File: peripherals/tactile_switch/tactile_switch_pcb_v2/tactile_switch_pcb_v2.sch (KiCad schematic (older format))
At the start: 3 parts, among them J1 PJ320A, SW1 SW_Push

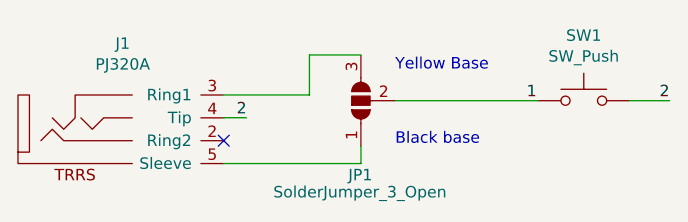
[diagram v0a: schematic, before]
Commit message: Increased tactile switch PCB hole diameters   - increased hole diameters to 1.2mm to accommodate pins     on 12mm x 12mm tactile switches.
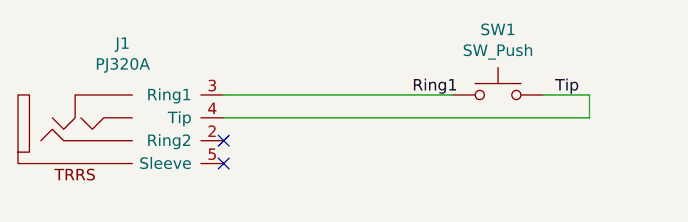
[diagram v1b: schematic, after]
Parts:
- removed JP1: SolderJumper_3_Open, Jumper:SolderJumper-3_P1.3mm_Open_RoundedPad1.0x1.5mm, symbol Jumper:SolderJumper_3_Open
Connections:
- net 1 is gone; now on net Ring1: SW1.1
- net Ring1: now reaches J1.3 (Ring1)
- net 2 renamed Tip
- no-connect marks 1 -> 2
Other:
- note removed: "Black base"
- note removed: "Yellow Base"
- moved on the sheet: SW1
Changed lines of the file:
@@
 EESchema Schematic File Version 4
-LIBS:tactile_switch_pcb_v2-cache
 EELAYER 30 0
 EELAYER END
@@
 L Switch:SW_Push SW1
 U 1 1 5D3251E9
-P 5950 3575
-F 0 "SW1" H 5950 3860 50  0000 C CNN
-F 1 "SW_Push" H 5950 3769 50  0000 C CNN
-F 2 "dbh_kicad_library:dbh_SW_PUSH-12mm" H 5950 3775 50  0001 C CNN
-F 3 "~" H 5950 3775 50  0001 C CNN
-	1    5950 3575
+P 5575 3550
+F 0 "SW1" H 5575 3835 50  0000 C CNN
+F 1 "SW_Push" H 5575 3744 50  0000 C CNN
+F 2 "dbh_kicad_library:dbh_SW_PUSH-12mm" H 5575 3750 50  0001 C CNN
+F 3 "~" H 5575 3750 50  0001 C CNN
+	1    5575 3550
 	1    0    0    -1
 $EndComp
-Wire Wire Line
-	6150 3575 6325 3575
-Text Label 6325 3575 2    50   ~ 0
-2
 $Comp
 L dbh_kicad_library:PJ320A J1
@@
 	1    0    0    -1
 $EndComp
+NoConn ~ 4375 3750
+Text Label 5200 3550 0    50   ~ 0
+Ring1
+NoConn ~ 4375 3850
 Wire Wire Line
-	4375 3650 4475 3650
-Text Label 4475 3650 2    50   ~ 0
-2
-NoConn ~ 4375 3750
-$Comp
-L Jumper:SolderJumper_3_Open JP1
-U 1 1 5D8354D3
-P 4975 3575
-F 0 "JP1" V 4650 3525 50  0000 L CNN
-F 1 "SolderJumper_3_Open" V 4575 3200 50  0000 L CNN
-F 2 "Jumper:SolderJumper-3_P1.3mm_Open_RoundedPad1.0x1.5mm" H 4975 3575 50  0001 C CNN
-F 3 "~" H 4975 3575 50  0001 C CNN
-	1    4975 3575
-	0    -1   -1   0
-$EndComp
+	4375 3550 5375 3550
 Wire Wire Line
-	5125 3575 5750 3575
+	5775 3550 5975 3550
 Wire Wire Line
-	4375 3550 4750 3550
+	5975 3550 5975 3650
 Wire Wire Line
-	4750 3550 4750 3375
-Wire Wire Line
-	4750 3375 4975 3375
-Text Notes 5125 3775 0    50   ~ 0
-Black base
-Text Notes 5125 3450 0    50   ~ 0
-Yellow Base
-Wire Wire Line
-	4375 3850 4975 3850
-Wire Wire Line
-	4975 3850 4975 3775
-Text Label 5700 3575 0    50   ~ 0
-1
+	5975 3650 4375 3650
+Text Label 5825 3550 0    50   ~ 0
+Tip
 $EndSCHEMATC
